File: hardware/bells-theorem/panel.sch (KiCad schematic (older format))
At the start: 79 parts, among them J10 D, J11 C, J12 DA, J13 CD, J14 DAB, J15 CDA, J16 A, J17 B, J18 AB, J19 BC, J20 ABC, J21 BCD, J22 left, J23 right, J4 IN, J5 CVA, J6 CVB, J7 CVC, J8 CVD, J9 ABCD, Q11 2N3904, Q2 2N3904, Q5 2N3904, Q8 2N3904

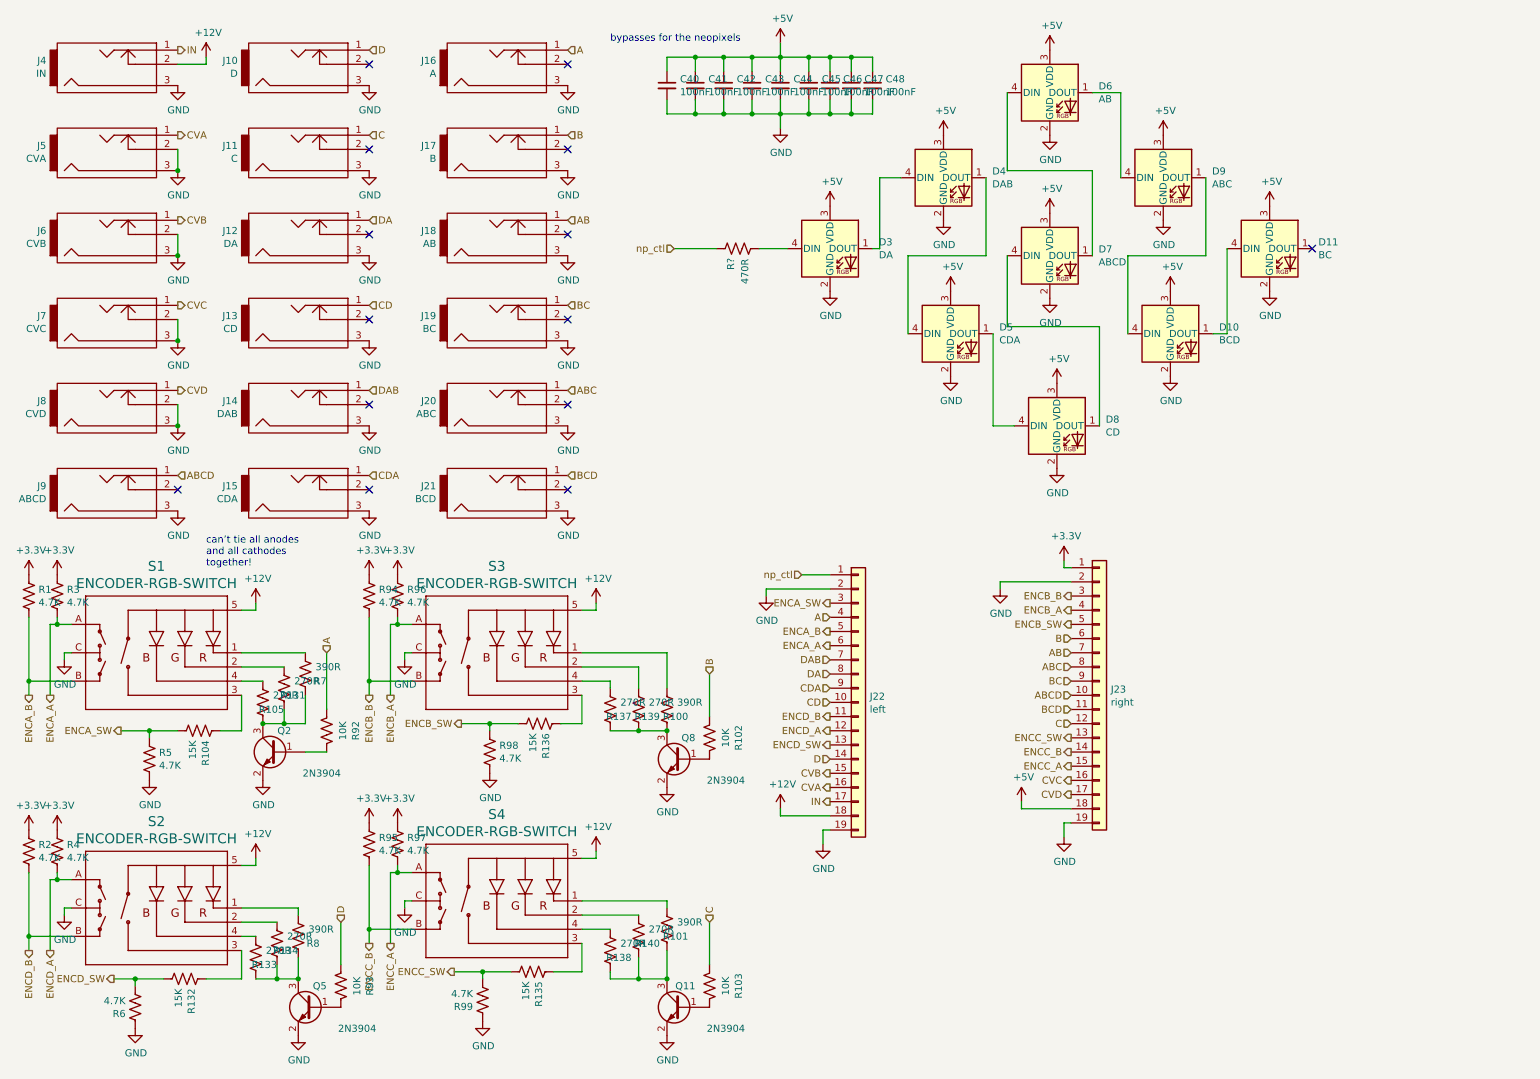
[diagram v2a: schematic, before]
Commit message: modified for Kicad 6 updated testing code
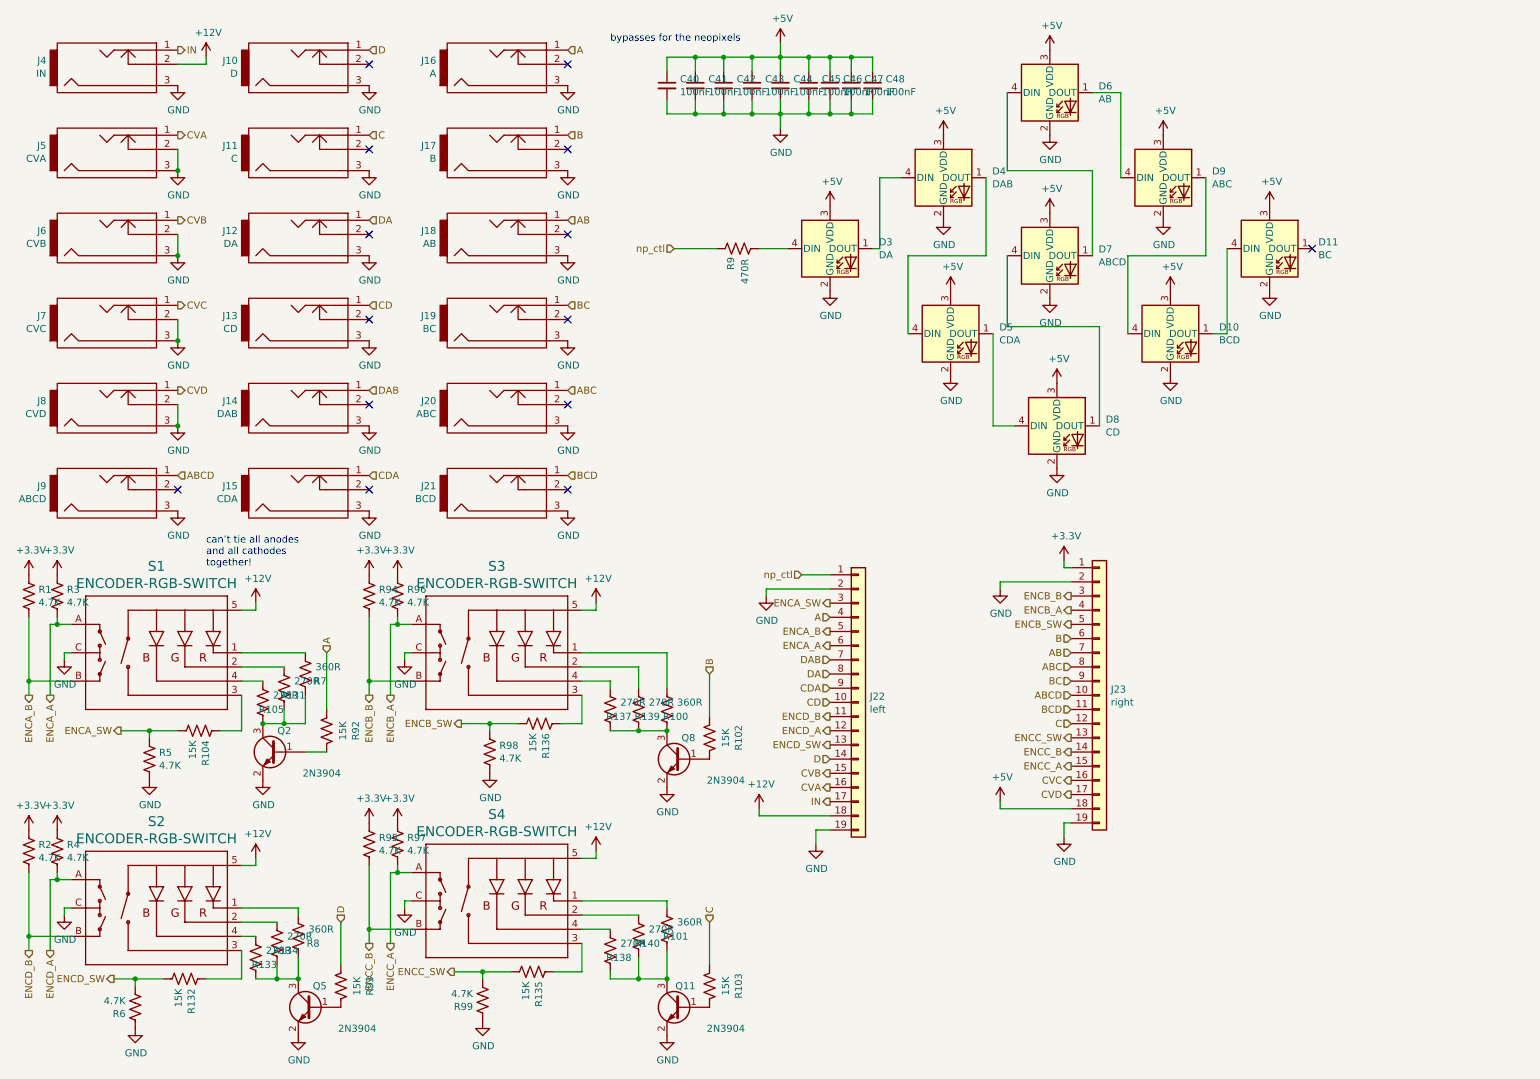
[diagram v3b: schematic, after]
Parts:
- J22, J23: footprint Connector_PinHeader_2.54mm:PinHeader_1x19_P2.54mm_Vertical -> (none)
- R100, R101, R7, R8: value 390R -> 360R
- R102, R103, R92, R93: value 10K -> 15K
- gave numbers to parts that had none: 1
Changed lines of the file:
@@
 L power:GND #PWR078
 U 1 1 5F889508
-P 6200 6300
+P 6150 6300
 AR Path="/5F7954A8/5F889508" Ref="#PWR078"  Part="1"
 AR Path="/5CEF66AD/5F889508" Ref="#PWR?"  Part="1"
-F 0 "#PWR078" H 6200 6050 50  0001 C CNN
-F 1 "GND" H 6205 6127 50  0000 C CNN
-F 2 "" H 6200 6300 50  0001 C CNN
-F 3 "" H 6200 6300 50  0001 C CNN
-	1    6200 6300
+F 0 "#PWR078" H 6150 6050 50  0001 C CNN
+F 1 "GND" H 6155 6127 50  0000 C CNN
+F 2 "" H 6150 6300 50  0001 C CNN
+F 3 "" H 6150 6300 50  0001 C CNN
+	1    6150 6300
 	1    0    0    -1
 $EndComp
@@
 L power:+12V #PWR077
 U 1 1 5F889514
-P 5900 6050
+P 5750 6050
 AR Path="/5F7954A8/5F889514" Ref="#PWR077"  Part="1"
 AR Path="/5CEF66AD/5F889514" Ref="#PWR?"  Part="1"
-F 0 "#PWR077" H 5900 5900 50  0001 C CNN
-F 1 "+12V" H 5915 6223 50  0000 C CNN
-F 2 "" H 5900 6050 50  0001 C CNN
-F 3 "" H 5900 6050 50  0001 C CNN
-	1    5900 6050
+F 0 "#PWR077" H 5750 5900 50  0001 C CNN
+F 1 "+12V" H 5765 6223 50  0000 C CNN
+F 2 "" H 5750 6050 50  0001 C CNN
+F 3 "" H 5750 6050 50  0001 C CNN
+	1    5750 6050
 	1    0    0    -1
 $EndComp
@@
 ENCA_A
 $Comp
-L Connectors_Generic:Conn_01x19 J?
-U 1 1 5F889538
-P 6450 5300
-AR Path="/5CEF66AD/5F889538" Ref="J?"  Part="1"
-AR Path="/5F7954A8/5F889538" Ref="J22"  Part="1"
-F 0 "J22" H 6530 5342 50  0000 L CNN
-F 1 "left" H 6530 5251 50  0000 L CNN
-F 2 "Connector_PinHeader_2.54mm:PinHeader_1x19_P2.54mm_Vertical" H 6450 5300 50  0001 C CNN
-F 3 "~" H 6450 5300 50  0001 C CNN
-	1    6450 5300
-	1    0    0    -1
-$EndComp
-$Comp
-L Connectors_Generic:Conn_01x19 J?
-U 1 1 5F88953E
-P 8150 5250
-AR Path="/5CEF66AD/5F88953E" Ref="J?"  Part="1"
-AR Path="/5F7954A8/5F88953E" Ref="J23"  Part="1"
-F 0 "J23" H 8230 5292 50  0000 L CNN
-F 1 "right" H 8230 5201 50  0000 L CNN
-F 2 "Connector_PinHeader_2.54mm:PinHeader_1x19_P2.54mm_Vertical" H 8150 5250 50  0001 C CNN
-F 3 "~" H 8150 5250 50  0001 C CNN
-	1    8150 5250
-	1    0    0    -1
-$EndComp
-$Comp
 L power:GND #PWR075
 U 1 1 5F88954A
@@
 	5800 4500 6250 4500
 Wire Wire Line
-	5900 6050 5900 6100
-Wire Wire Line
-	5900 6100 6250 6100
-Wire Wire Line
-	6200 6300 6200 6200
-Wire Wire Line
-	6200 6200 6250 6200
+	5750 6050 5750 6100
+Wire Wire Line
+	5750 6100 6250 6100
 $Comp
 L power:GND #PWR079
@@
 	7450 4450 7950 4450
 Wire Wire Line
-	7600 6000 7600 6050
-Wire Wire Line
-	7600 6050 7950 6050
+	7450 6000 7450 6050
 Wire Wire Line
 	7900 6250 7900 6150
@@
 P 5400 5550
 F 0 "R102" V 5195 5550 50  0000 C CNN
-F 1 "10K" V 5286 5550 50  0000 C CNN
+F 1 "15K" V 5286 5550 50  0000 C CNN
 F 2 "Resistor_SMD:R_0805_2012Metric_Pad1.15x1.40mm_HandSolder" V 5440 5540 50  0001 C CNN
 F 3 "~" H 5400 5550 50  0001 C CNN
@@
 P 5400 7300
 F 0 "R103" V 5195 7300 50  0000 C CNN
-F 1 "10K" V 5286 7300 50  0000 C CNN
+F 1 "15K" V 5286 7300 50  0000 C CNN
 F 2 "Resistor_SMD:R_0805_2012Metric_Pad1.15x1.40mm_HandSolder" V 5440 7290 50  0001 C CNN
 F 3 "~" H 5400 7300 50  0001 C CNN
@@
 P 2800 7300
 F 0 "R93" V 2595 7300 50  0000 C CNN
-F 1 "10K" V 2686 7300 50  0000 C CNN
+F 1 "15K" V 2686 7300 50  0000 C CNN
 F 2 "Resistor_SMD:R_0805_2012Metric_Pad1.15x1.40mm_HandSolder" V 2840 7290 50  0001 C CNN
 F 3 "~" H 2800 7300 50  0001 C CNN
@@
 P 2700 5500
 F 0 "R92" V 2495 5500 50  0000 C CNN
-F 1 "10K" V 2586 5500 50  0000 C CNN
+F 1 "15K" V 2586 5500 50  0000 C CNN
 F 2 "Resistor_SMD:R_0805_2012Metric_Pad1.15x1.40mm_HandSolder" V 2740 5490 50  0001 C CNN
 F 3 "~" H 2700 5500 50  0001 C CNN
@@
 P 2500 6950
 F 0 "R8" H 2350 7000 50  0000 L CNN
-F 1 "390R" H 2250 6900 50  0000 L CNN
+F 1 "360R" H 2250 6900 50  0000 L CNN
 F 2 "Resistor_SMD:R_0805_2012Metric_Pad1.15x1.40mm_HandSolder" V 2540 6940 50  0001 C CNN
 F 3 "~" H 2500 6950 50  0001 C CNN
@@
 P 5100 6900
 F 0 "R101" H 4950 6950 50  0000 L CNN
-F 1 "390R" H 4850 6850 50  0000 L CNN
+F 1 "360R" H 4850 6850 50  0000 L CNN
 F 2 "Resistor_SMD:R_0805_2012Metric_Pad1.15x1.40mm_HandSolder" V 5140 6890 50  0001 C CNN
 F 3 "~" H 5100 6900 50  0001 C CNN
@@
 P 5100 5350
 F 0 "R100" H 4950 5400 50  0000 L CNN
-F 1 "390R" H 4850 5300 50  0000 L CNN
+F 1 "360R" H 4850 5300 50  0000 L CNN
 F 2 "Resistor_SMD:R_0805_2012Metric_Pad1.15x1.40mm_HandSolder" V 5140 5340 50  0001 C CNN
 F 3 "~" H 5100 5350 50  0001 C CNN
@@
 P 2550 5100
 F 0 "R7" H 2400 5150 50  0000 L CNN
-F 1 "390R" H 2300 5050 50  0000 L CNN
+F 1 "360R" H 2300 5050 50  0000 L CNN
 F 2 "Resistor_SMD:R_0805_2012Metric_Pad1.15x1.40mm_HandSolder" V 2590 5090 50  0001 C CNN
 F 3 "~" H 2550 5100 50  0001 C CNN
@@
 L power:+5V #PWR0163
 U 1 1 60767615
-P 7600 6000
-F 0 "#PWR0163" H 7600 5850 50  0001 C CNN
-F 1 "+5V" H 7615 6173 50  0000 C CNN
-F 2 "" H 7600 6000 50  0001 C CNN
-F 3 "" H 7600 6000 50  0001 C CNN
-	1    7600 6000
+P 7450 6000
+F 0 "#PWR0163" H 7450 5850 50  0001 C CNN
+F 1 "+5V" H 7465 6173 50  0000 C CNN
+F 2 "" H 7450 6000 50  0001 C CNN
+F 3 "" H 7450 6000 50  0001 C CNN
+	1    7450 6000
 	1    0    0    -1
 $EndComp
@@
 	5950 2100 5750 2100
 $Comp
-L device:R_US R?
+L device:R_US R9
 U 1 1 6155FA0B
 P 5600 2100
-F 0 "R?" H 5450 2150 50  0000 L CNN
+F 0 "R9" H 5450 2150 50  0000 L CNN
 F 1 "470R" H 5350 2050 50  0000 L CNN
 F 2 "Resistor_SMD:R_0805_2012Metric_Pad1.15x1.40mm_HandSolder" V 5640 2090 50  0001 C CNN
@@
 Wire Wire Line
 	5150 2100 5450 2100
+Wire Wire Line
+	7450 6050 7950 6050
+$Comp
+L Connectors_Generic:Conn_01x19 J23
+U 1 1 615CBD34
+P 8150 5250
+F 0 "J23" H 8230 5292 50  0000 L CNN
+F 1 "right" H 8230 5201 50  0000 L CNN
+F 2 "" H 8150 5250 50  0001 C CNN
+F 3 "~" H 8150 5250 50  0001 C CNN
+	1    8150 5250
+	1    0    0    -1
+$EndComp
+$Comp
+L Connectors_Generic:Conn_01x19 J22
+U 1 1 615ED511
+P 6450 5300
+F 0 "J22" H 6530 5342 50  0000 L CNN
+F 1 "left" H 6530 5251 50  0000 L CNN
+F 2 "" H 6450 5300 50  0001 C CNN
+F 3 "~" H 6450 5300 50  0001 C CNN
+	1    6450 5300
+	1    0    0    -1
+$EndComp
+Wire Wire Line
+	6150 6300 6150 6200
+Wire Wire Line
+	6150 6200 6250 6200
 $EndSCHEMATC
